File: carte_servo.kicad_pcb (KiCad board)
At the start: 4 copper layers, 53.8 x 106.7 mm, 128 parts, among them J1 Conn_Arduino_Power, J10 Conn_01x03_Male, J11 Transistor_2, J12 Transistor_1, J13 Transistor_4, J14 Transistor_.3, J15 12V_BATT, J16 Conn_01x04_Male, J17 Conn_01x04_Male, J18 Conn_01x03_Male, J19 Conn_01x03_Male, J2 Conn_Arduino_A0_A7, J20 Stepper, J21 Stepper, J22 SPI_RFID, J23 12V_BATT, J24 Conn_LEDs, J25 Conn_AX12, J26 Conn_Arduino_A8_A15, J27 Conn_Arduino_D21_D14, J28 Conn_Arduino_D22_D53, J29 Conn_AX12, J3 Conn_Arduino_D8_D13, J30 12V_BATT, J4 Conn_Arduino_D0_D7, J5 Conn_01x03_Male, J6 Conn_01x03_Male, J7 Conn_01x03_Male, J8 Conn_01x03_Male, J9 Conn_01x03_Male, Q1 DMN2011UTS, Q2 DMN2011UTS, Q3 DMN2011UTS, Q4 DMN2011UTS, Q5 DMN2011UTS, Q6 DMN2011UTS, U1 XGZP6897D_differential_pressu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, U2 XGZP6897D_differential_pressu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, U3 TMC2208_SILENTSTEPSTICK, U4 TMC2208_SILENTSTEPSTICK, U5 74LVC2G241

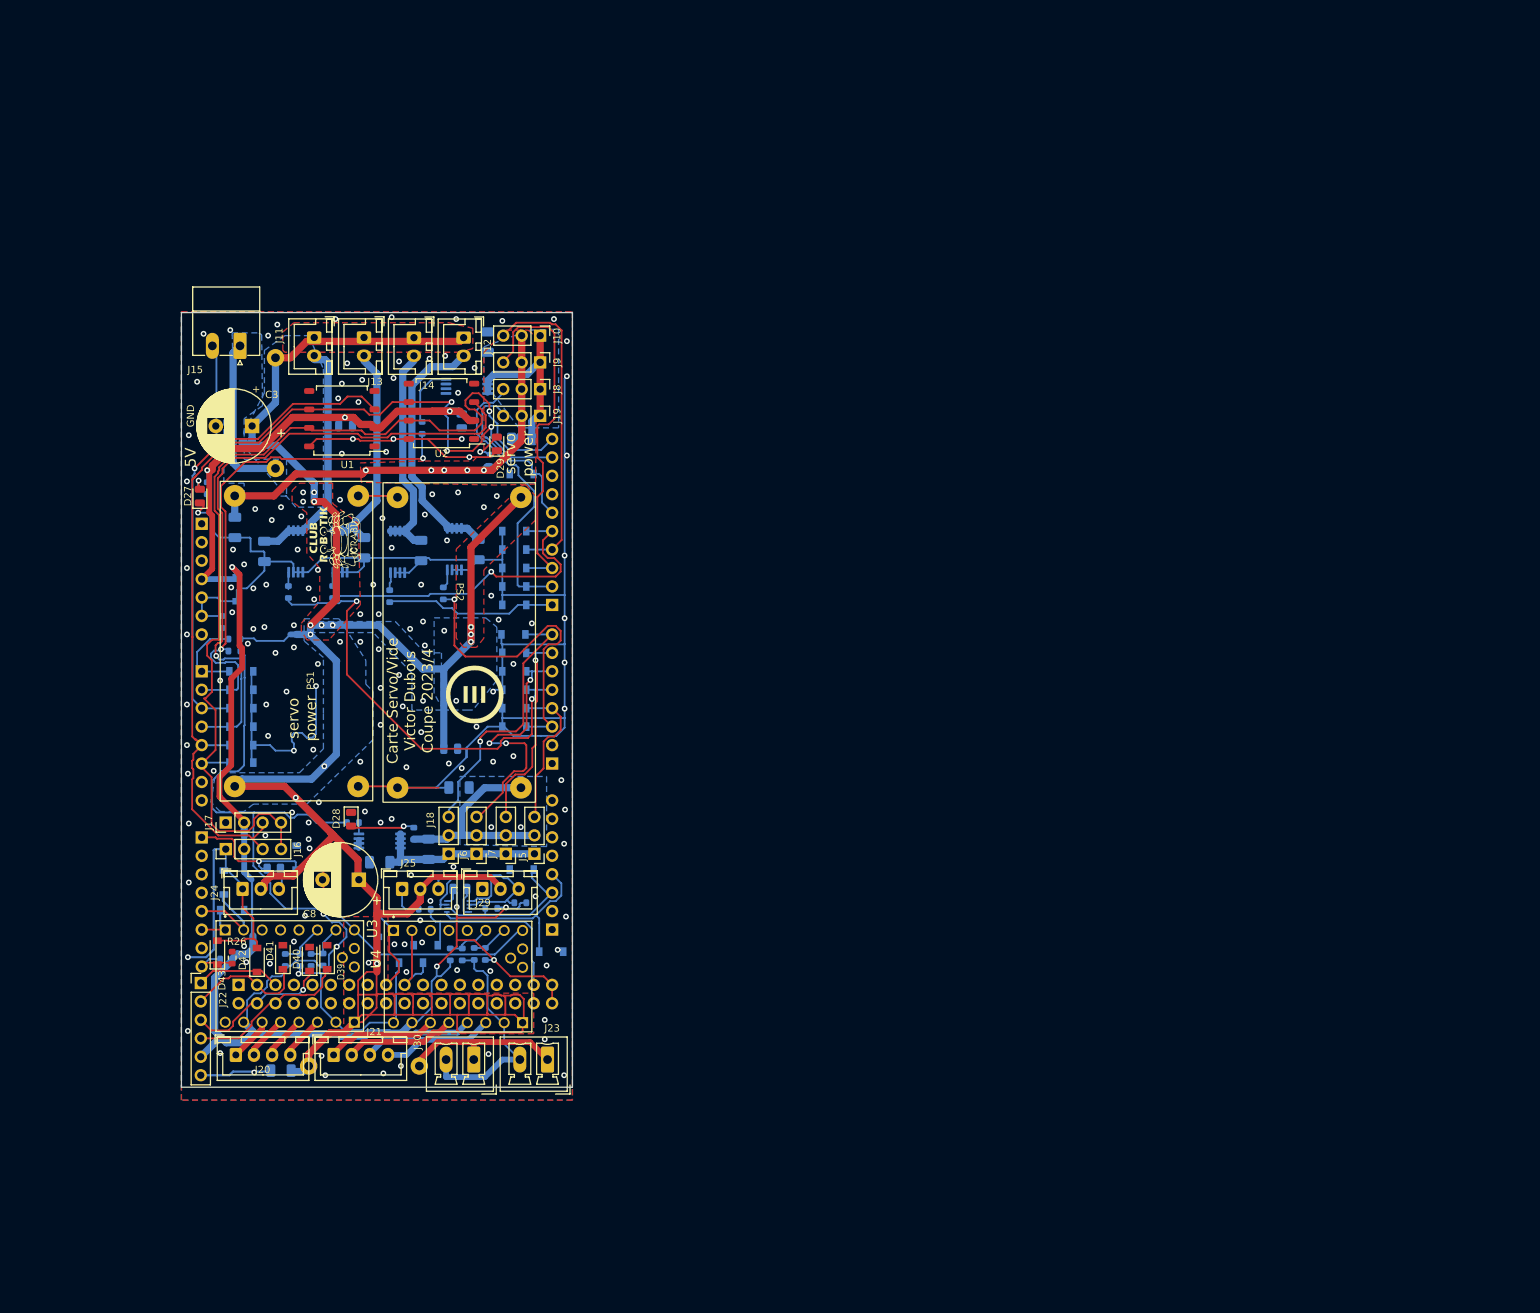
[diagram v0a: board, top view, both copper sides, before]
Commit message: WiP start switching to an ESP32
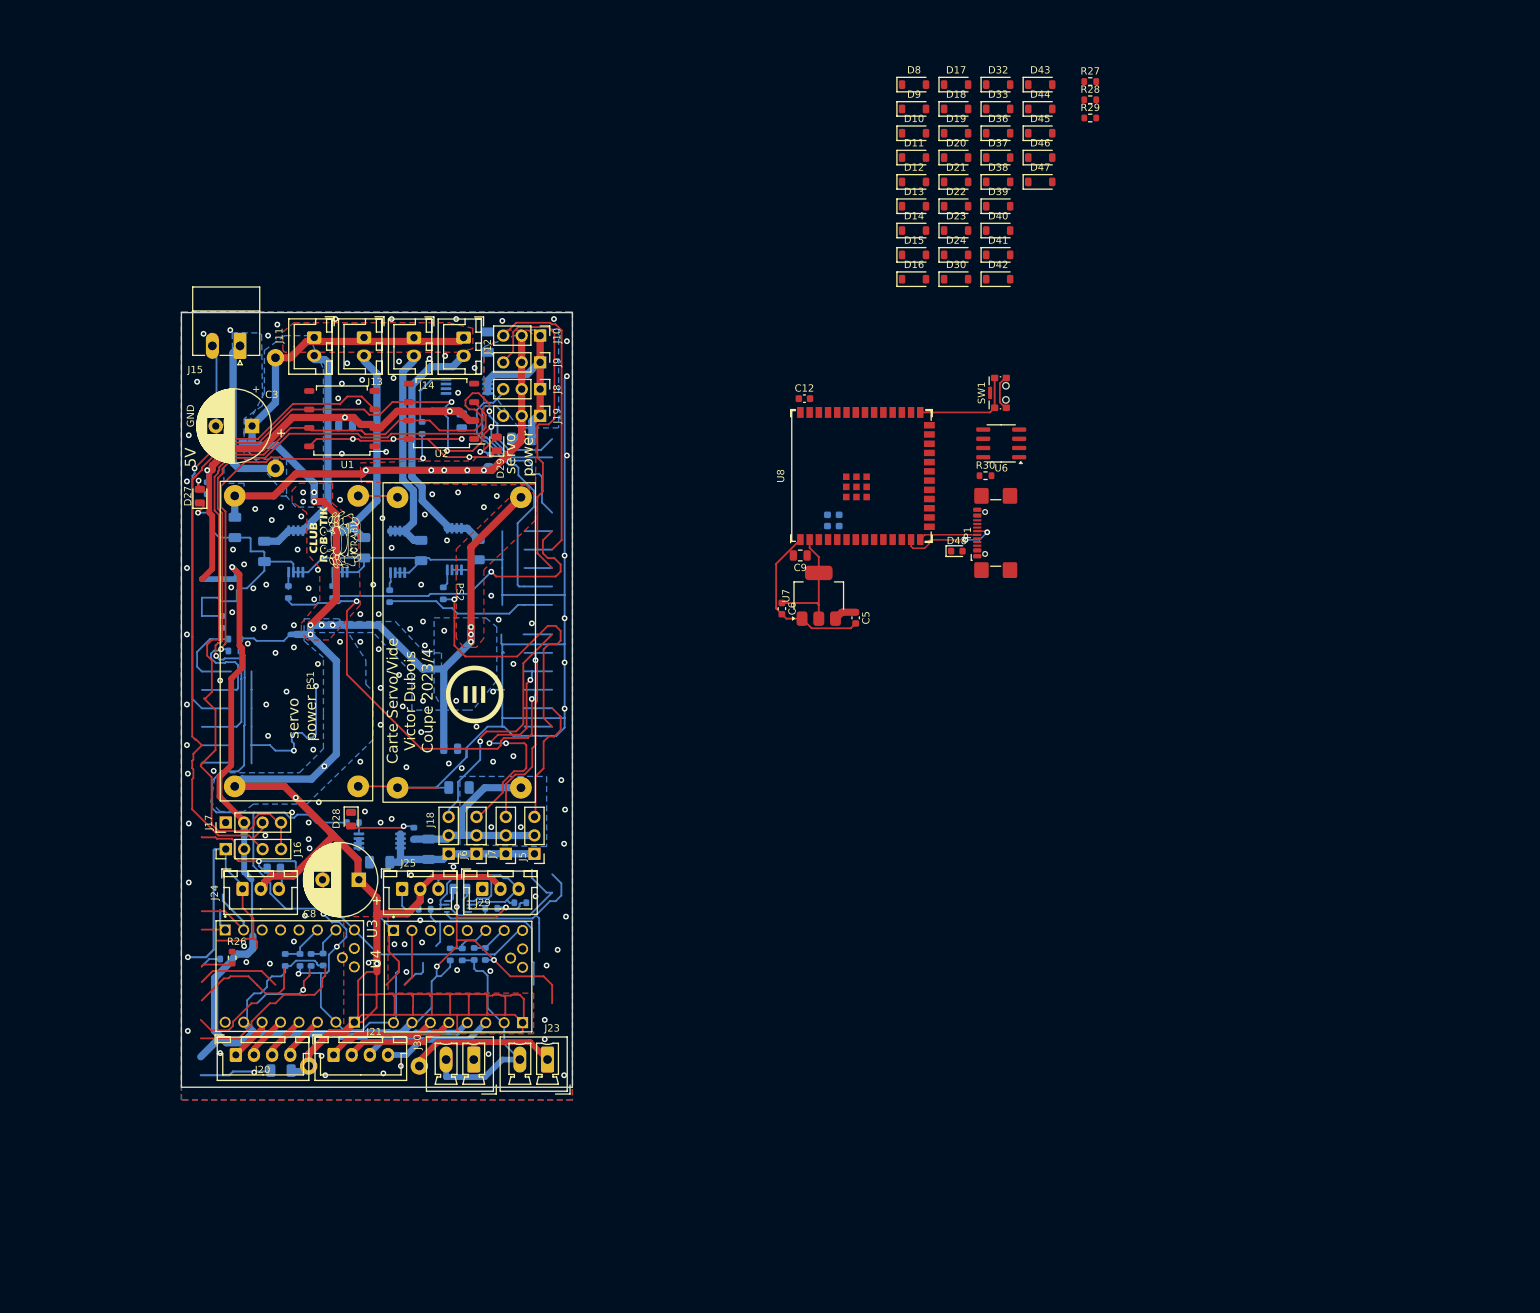
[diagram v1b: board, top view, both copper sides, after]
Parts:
- removed J1: Conn_Arduino_Power, Connector_PinHeader_2.54mm:PinHeader_1x07_P2.54mm_Vertical
- removed J2: Conn_Arduino_A0_A7, Connector_PinHeader_2.54mm:PinHeader_1x08_P2.54mm_Vertical
- removed J22: SPI_RFID, Connector_PinHeader_2.54mm:PinHeader_1x06_P2.54mm_Vertical
- removed J26: Conn_Arduino_A8_A15, Connector_PinHeader_2.54mm:PinHeader_1x08_P2.54mm_Vertical
- removed J27: Conn_Arduino_D21_D14, Connector_PinHeader_2.54mm:PinHeader_1x08_P2.54mm_Vertical
- removed J28: Conn_Arduino_D22_D53, Connector_PinHeader_2.54mm:PinHeader_2x18_P2.54mm_Vertical
- removed J3: Conn_Arduino_D8_D13, Connector_PinHeader_2.54mm:PinHeader_1x10_P2.54mm_Vertical
- removed J4: Conn_Arduino_D0_D7, Connector_PinHeader_2.54mm:PinHeader_1x08_P2.54mm_Vertical
- removed locked: D_Zener_Small, Diode_SMD:D_SOD-123
- added C10: 100nF, Capacitor_SMD:C_0603_1608Metric, B.Cu at (170.0, 87.2)
- added C11: 100nF, Capacitor_SMD:C_0603_1608Metric, B.Cu at (171.6, 87.2)
- added C12: 100nF, Capacitor_SMD:C_0603_1608Metric, F.Cu at (166.8, 70.4)
- added C5: 1µF, Capacitor_SMD:C_0603_1608Metric, F.Cu at (173.9, 100.6)
- added C6: 4.7µF, Capacitor_SMD:C_0603_1608Metric, F.Cu at (163.7, 99.3)
- added C9: 10µF, Capacitor_SMD:C_0805_2012Metric, F.Cu at (166.2, 92.0)
- added D48: D, Diode_SMD:D_0603_1608Metric, F.Cu at (187.8, 91.4)
- added D8: D_Zener_Small, Diode_SMD:D_SOD-123, F.Cu at (181.9, 27.1)
- added P1: USB_C_Plug_USB2.0, Connector_USB:USB_C_Receptacle_GCT_USB4110, F.Cu at (194.3, 88.9)
- added R27: 5.11kR, Resistor_SMD:R_0603_1608Metric, F.Cu at (206.2, 26.7)
- added R28: 1MR, Resistor_SMD:R_0603_1608Metric, F.Cu at (206.2, 29.2)
- added R29: 5.11kR, Resistor_SMD:R_0603_1608Metric, F.Cu at (206.2, 31.8)
- added R30: 22kR, Resistor_SMD:R_0603_1608Metric, F.Cu at (191.8, 81.0)
- added SW1: CK_KMS2xxG, Button_Switch_SMD:SW_SPST_CK_KMS2xxGP, F.Cu at (193.8, 69.6)
- added U6: SN65HVD230, Package_SO:SOIC-8_3.9x4.9mm_P1.27mm, F.Cu at (193.9, 76.6)
- added U7: LD1117S33TR_SOT223, Package_TO_SOT_SMD:SOT-223-3_TabPin2, F.Cu at (168.8, 97.5)
- added U8: ESP32-S3-WROOM-1, PCM_Espressif:ESP32-S3-WROOM-1U, F.Cu at (174.5, 81.0)
- D10, D11, D12, D13, D14, D15, D16, D17, D18, D19, D20, D21, D22, D23, D24, D30, D32, D33, D36, D37, D38, D44, D45, D46, D47, D9: moved to F.Cu
- moved D43 164.7 mm to (199.3, 27.1), turned to 0 degrees
- moved D46 152.1 mm to (199.3, 37.2)
- moved D47 148.2 mm to (199.3, 40.5), turned to 0 degrees
- moved D44 146.1 mm to (199.3, 30.5), turned to 0 degrees
- moved D45 142.2 mm to (199.3, 33.9), turned to 0 degrees
- moved D39 138.7 mm to (193.5, 43.9), turned to 0 degrees
- moved D42 138.6 mm to (193.5, 54.0), turned to 0 degrees
- moved D41 138.1 mm to (193.5, 50.6), turned to 0 degrees
- moved D40 138.1 mm to (193.5, 47.2), turned to 0 degrees
- moved D17 132.3 mm to (187.7, 27.1)
- moved D38 131.4 mm to (193.5, 40.5), turned to 0 degrees
- moved D37 125.5 mm to (193.5, 37.2)
- moved D30 120.8 mm to (187.7, 54.0), turned to 0 degrees
- moved D36 120.8 mm to (193.5, 33.9), turned to 0 degrees
- moved D18 119.1 mm to (187.7, 30.5), turned to 0 degrees
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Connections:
- D10 pad 1: SERVO_3 -> DIR_1
- D11 pad 1: SERVO_4 -> STEP_1
- D12 pad 1: SERVO_5 -> sense_5V
- D13 pad 1: SERVO_6 -> LEDs
- D14 pad 1: SDA -> AX12_master_RX
- D15 pad 1: SCL -> AX12_master_TX
- D16 pad 1: Pressure_1 -> AX12_tx_en
- D17 pad 1: Pressure_2 -> SPI_MOSI
- D18 pad 1: 5V -> SPI_SS
- D19 pad 1: TRANSISTOR_1 -> SPI_SCK
- D20 pad 1: TRANSISTOR_2 -> SPI_MISO
- D21 pad 1: TRANSISTOR_3 -> SERVO_7
- D22 pad 1: TRANSISTOR_4 -> SERVO_8
- D23 pad 1: A0 -> SERVO_1
- D24 pad 1: ENABLE_SERVO_POWER_2 -> SERVO_2
- D30 pad 1: LEDs -> SERVO_3
- D32 pad 1: SERVO_7 -> SERVO_4
- D33 pad 1: SERVO_8 -> SERVO_5
- D36 pad 1: AX12_master_RX -> SERVO_6
- D37 pad 1: AX12_master_TX -> SDA
- D38 pad 1: AX12_tx_en -> SCL
- D39 pad 1: SPI_MOSI -> Pressure_1
- D40 pad 1: SPI_SS -> Pressure_2
- D41 pad 1: SPI_SCK -> 5V
- D42 pad 1: SPI_MISO -> TRANSISTOR_1
- D43 pad 1: A15 -> TRANSISTOR_2
- D44 pad 1: STEP_2 -> TRANSISTOR_3
- D45 pad 1: DIR_2 -> TRANSISTOR_4
- D46 pad 1: DIR_1 -> sense_12V
- D47 pad 1: STEP_1 -> ENABLE_SERVO_POWER_2
- D9 pad 1: SERVO_2 -> DIR_2
- R25 pad 2: A15 -> sense_5V
- R26 pad 1: A15 -> sense_5V
- R8 pad 2: A0 -> sense_12V
- R9 pad 1: A0 -> sense_12V
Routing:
- net GND: track 451.3 -> 479.5 mm
- net 3.3V: track 0.00 -> 16.6 mm
- net BOOT: track 0.00 -> 14.6 mm
- net D-: track 0.00 -> 14.1 mm, vias 0 -> 2
- net sense_12V: track 0.00 -> 13.6 mm
- net A0: track 13.6 -> 0.00 mm
- net D+: track 0.00 -> 8.12 mm
- net A15: track 7.42 -> 0.00 mm
- net sense_5V: track 0.00 -> 7.32 mm
- net 5V: track 256.2 -> 259.4 mm

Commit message: start placing components from scratch
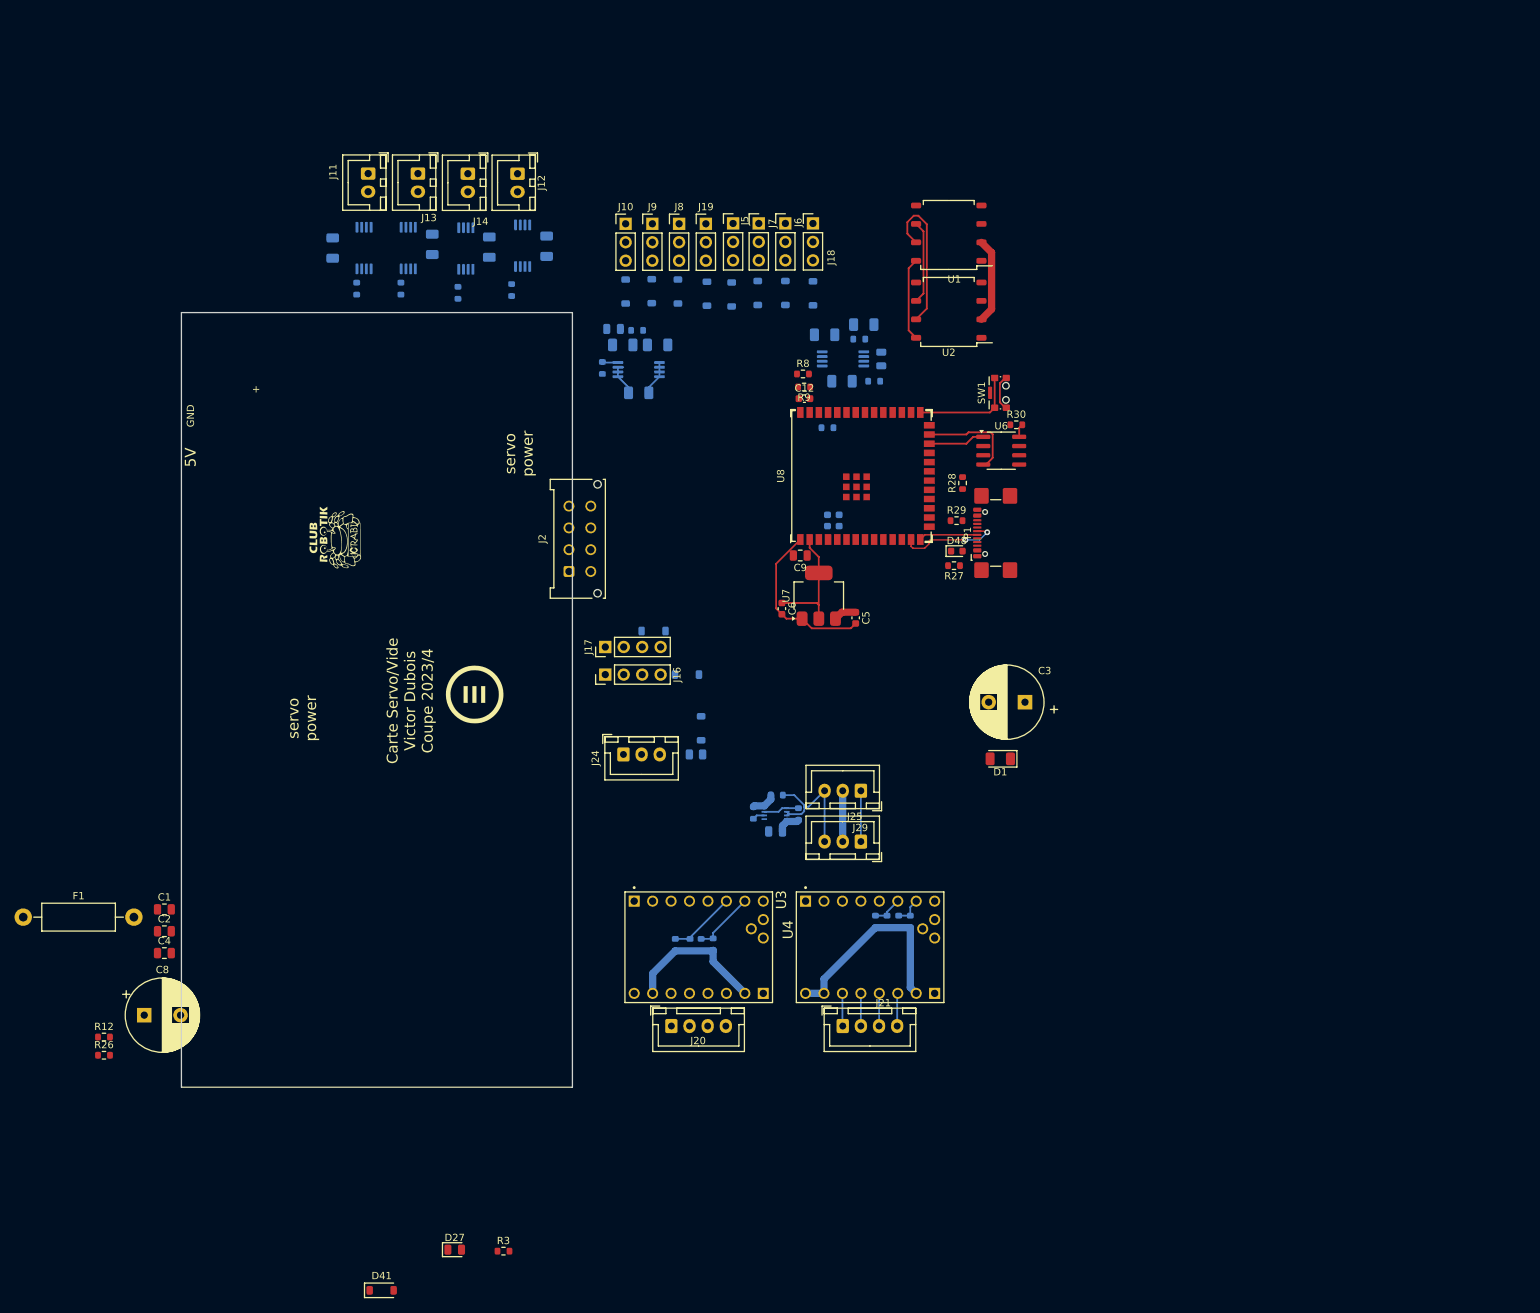
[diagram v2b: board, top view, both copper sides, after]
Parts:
- removed D10, D11, D12, D14, D15, D16, D17, D18, D19, D20, D39, D40, D42, D43, D44, D45, D46, D47, D8, D9: D_Zener_Small, Diode_SMD:D_SOD-123
- removed D31: 13V, Diode_SMD:D_1206_3216Metric
- removed F3: Fuse, Resistor_THT:R_Axial_DIN0411_L9.9mm_D3.6mm_P15.24mm_Horizontal
- removed J15: 12V_BATT, Connector_Phoenix_MC:PhoenixContact_MC_1,5_2-G-3.81_1x02_P3.81mm_Horizontal
- removed J23, J30: 12V_BATT, Connector_Phoenix_MC:PhoenixContact_MCV_1,5_2-G-3.81_1x02_P3.81mm_Vertical
- removed PS1, PS2: LM2596s module, LibraryVictor:lm2596Module
- added J2: Conn_02x04_Top_Bottom, Connector_Molex:Molex_Micro-Fit_3.0_43045-0812_2x04_P3.00mm_Vertical, F.Cu at (134.4, 94.2)
- C1, C2, C4, D1, F1, R12, R3, R8, R9: moved to F.Cu
- D13, D21, D22, D23, D24, D28, D29, D30, D32, D33, D36, D37, D38: moved to B.Cu
- moved D41 166.0 mm to (108.6, 193.2)
- moved D1 114.1 mm to (193.8, 120.0)
- moved C3 113.0 mm to (197.2, 112.2)
- moved R3 112.7 mm to (125.4, 187.8), turned to 0 degrees
- moved R25 110.5 mm to (170.0, 74.4)
- moved D27 109.6 mm to (118.7, 187.6), turned to 0 degrees
- moved J18 100.3 mm to (168.0, 46.3), turned to 0 degrees
- moved J6 96.7 mm to (164.2, 46.3), turned to 0 degrees
- moved J7 93.5 mm to (160.5, 46.3), turned to 0 degrees
- moved J5 91.0 mm to (157.0, 46.3), turned to 0 degrees
- moved D3 91.0 mm to (175.0, 60.2), turned to 0 degrees
- moved U1 87.4 mm to (186.7, 47.6)
- moved R9 86.4 mm to (166.8, 68.8), turned to 180 degrees
- moved R8 86.4 mm to (166.6, 67.0), turned to 0 degrees
- moved F1 84.5 mm to (59.2, 141.8), turned to 0 degrees
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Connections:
- F1 pad 2: 12V_before_fuse -> 12V_ELEC_P
- U6 pad 6: CANL -> CAN_L
- U6 pad 7: CANH -> CAN_H
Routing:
- net GND: track 479.5 -> 54.9 mm, vias 160 -> 0
- net BATT_12V: track 369.2 -> 7.00 mm, vias 18 -> 0
- net 5V: track 259.4 -> 67.1 mm, vias 8 -> 0
- net SDA: track 133.4 -> 11.4 mm, vias 3 -> 0
- net SCL: track 136.5 -> 20.5 mm, vias 1 -> 0
- net ENABLE_SERVO_POWER_1: track 96.6 -> 0.00 mm
- net Pressure_2: track 88.3 -> 0.00 mm, vias 1 -> 0
- net ENABLE_SERVO_POWER_2: track 71.9 -> 0.00 mm, vias 2 -> 0
- net Pressure_1: track 67.1 -> 0.00 mm, vias 1 -> 0
- net SERVO_POWER_2: track 65.4 -> 0.00 mm, vias 5 -> 0
- net TRANSISTOR_2: track 61.5 -> 0.00 mm, vias 2 -> 0
- net SERVO_5: track 50.3 -> 0.00 mm
- net TRANSISTOR_4: track 44.9 -> 0.00 mm, vias 1 -> 0
- net TRANSISTOR_1: track 44.3 -> 0.00 mm, vias 1 -> 0
- net SERVO_6: track 43.8 -> 0.00 mm
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- removed copper zone on B.Cu, net 12V_before_fuse
- removed copper zone on In2.Cu, net 12V_before_fuse
- removed copper zone on In2.Cu, net 5V
- removed copper zone on B.Cu, net BATT_12V
- removed copper zone on F.Cu, net BATT_12V
- removed copper zone on In2.Cu, net BATT_12V
- removed copper zone on B.Cu, net GND
- removed copper zone on F.Cu, net GND
- removed copper zone on In1.Cu, net GND
- removed copper zone on In2.Cu, net GND
- removed copper zone on B.Cu, net GND_SERVO_2
- removed copper zone on B.Cu, net SERVO_POWER_1
- removed copper zone on In2.Cu, net SERVO_POWER_1
- removed copper zone on F.Cu, net SERVO_POWER_2
- removed copper zone on In2.Cu, net SERVO_POWER_2
